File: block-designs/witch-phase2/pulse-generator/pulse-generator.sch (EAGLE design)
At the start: 63 parts, among them IC1 74LVC1G08DBV, IC10 74LVC1G08DBV, IC11 741G175, IC12 74LVC1G08DBV, IC13 741G175, IC14 741G175, IC15 741G175, IC16 74LVC1G04DBV, IC17 741G175, IC18 74LVC1G04DBV, IC19 74LVC1G04DBV, IC2 741G175, IC20 NE555D, IC21 74LVC1G17DBV, IC22 74LVC1G17DBV, IC23 74LVC1G17DBV, IC3 741G175, IC4 741G175, IC5 74LVC1G04DBV, IC6 74LVC1G08DBV, IC7 741G175, IC8 74LVC1G08DBV, IC9 74LVC1G08DBV, J1 POWER_JACKPTH, Q1 MMBT2907ALT1SMD

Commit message: add dekatron sim connector and silkscreen cleanup
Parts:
- added JP3: (no value), pinhead:PINHD-1X4
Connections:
- net 10A_PULSE: now also JP3.2
- net GND: now also J1.GND, J1.GNDBREAK, JP3.4; no longer J1.PWR
- net VCC: now also J1.PWR, JP3.1; no longer J1.GND, J1.GNDBREAK
- net ZC: now also JP3.3
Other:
- moved on the sheet: J1
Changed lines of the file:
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@@
 <layer number="132" name="bAdjust" color="7" fill="1" visible="yes" active="yes"/>
 <layer number="144" name="Drill_legend" color="7" fill="1" visible="yes" active="yes"/>
+<layer number="145" name="DrillLegend_01-16" color="2" fill="9" visible="yes" active="yes"/>
 <layer number="150" name="Notes" color="7" fill="1" visible="yes" active="yes"/>
 <layer number="151" name="HeatSink" color="7" fill="1" visible="yes" active="yes"/>
@@
 <part name="IC23" library="74xx-little-us" deviceset="74*1G17" device="DBV" technology="LVC"/>
 <part name="JP1" library="pinhead" deviceset="PINHD-1X11" device=""/>
+<part name="GND13" library="supply1" deviceset="GND" device=""/>
+<part name="JP3" library="pinhead" deviceset="PINHD-1X4" device=""/>
+<part name="P+17" library="supply1" deviceset="VCC" device=""/>
 </parts>
 <sheets>
@@
 <instance part="FRAME1" gate="G$1" x="0" y="0"/>
 <instance part="FRAME1" gate="G$2" x="299.72" y="0"/>
-<instance part="J1" gate="G$1" x="29.21" y="33.02" rot="MR180"/>
+<instance part="J1" gate="G$1" x="30.48" y="20.32"/>
 <instance part="P+10" gate="VCC" x="41.91" y="39.37" rot="MR0"/>
 <instance part="GND10" gate="1" x="41.91" y="16.51" rot="MR0"/>
@@
 <instance part="IC23" gate="G$1" x="73.66" y="171.45"/>
 <instance part="JP1" gate="A" x="370.84" y="123.19"/>
+<instance part="GND13" gate="1" x="358.14" y="181.61"/>
+<instance part="JP3" gate="A" x="368.3" y="194.31"/>
+<instance part="P+17" gate="VCC" x="358.14" y="209.55"/>
 </instances>
 <busses>
@@
 <net name="VCC" class="0">
 <segment>
-<pinref part="J1" gate="G$1" pin="GNDBREAK"/>
-<wire x1="31.75" y1="27.94" x2="41.91" y2="27.94" width="0.1524" layer="91"/>
-<wire x1="41.91" y1="27.94" x2="41.91" y2="30.48" width="0.1524" layer="91"/>
-<pinref part="J1" gate="G$1" pin="GND"/>
-<wire x1="41.91" y1="30.48" x2="41.91" y2="36.83" width="0.1524" layer="91"/>
-<wire x1="31.75" y1="30.48" x2="41.91" y2="30.48" width="0.1524" layer="91"/>
-<junction x="41.91" y="30.48"/>
-<junction x="41.91" y="27.94"/>
+<wire x1="41.91" y1="27.94" x2="41.91" y2="36.83" width="0.1524" layer="91"/>
 <pinref part="P+10" gate="VCC" pin="VCC"/>
 <pinref part="JP2" gate="G$1" pin="1"/>
 <wire x1="41.91" y1="27.94" x2="50.8" y2="27.94" width="0.1524" layer="91"/>
+<pinref part="J1" gate="G$1" pin="PWR"/>
+<wire x1="41.91" y1="27.94" x2="33.02" y2="27.94" width="0.1524" layer="91"/>
+<junction x="41.91" y="27.94"/>
 </segment>
 <segment>
@@
 <wire x1="33.02" y1="184.15" x2="33.02" y2="186.69" width="0.1524" layer="91"/>
 </segment>
+<segment>
+<wire x1="365.76" y1="199.39" x2="358.14" y2="199.39" width="0.1524" layer="91"/>
+<wire x1="358.14" y1="199.39" x2="358.14" y2="207.01" width="0.1524" layer="91"/>
+<pinref part="JP3" gate="A" pin="1"/>
+<pinref part="P+17" gate="VCC" pin="VCC"/>
+</segment>
 </net>
 <net name="GND" class="0">
 <segment>
-<pinref part="J1" gate="G$1" pin="PWR"/>
-<wire x1="31.75" y1="25.4" x2="41.91" y2="25.4" width="0.1524" layer="91"/>
-<wire x1="41.91" y1="25.4" x2="41.91" y2="19.05" width="0.1524" layer="91"/>
+<wire x1="41.91" y1="25.4" x2="41.91" y2="22.86" width="0.1524" layer="91"/>
 <pinref part="GND10" gate="1" pin="GND"/>
 <pinref part="JP2" gate="G$1" pin="2"/>
+<wire x1="41.91" y1="22.86" x2="41.91" y2="19.05" width="0.1524" layer="91"/>
 <wire x1="41.91" y1="25.4" x2="50.8" y2="25.4" width="0.1524" layer="91"/>
+<pinref part="J1" gate="G$1" pin="GNDBREAK"/>
+<wire x1="41.91" y1="25.4" x2="33.02" y2="25.4" width="0.1524" layer="91"/>
+<pinref part="J1" gate="G$1" pin="GND"/>
+<wire x1="33.02" y1="22.86" x2="41.91" y2="22.86" width="0.1524" layer="91"/>
 <junction x="41.91" y="25.4"/>
+<junction x="41.91" y="22.86"/>
 </segment>
 <segment>
@@
 <junction x="16.51" y="171.45"/>
 </segment>
+<segment>
+<wire x1="358.14" y1="191.77" x2="358.14" y2="184.15" width="0.1524" layer="91"/>
+<pinref part="GND13" gate="1" pin="GND"/>
+<wire x1="358.14" y1="191.77" x2="365.76" y2="191.77" width="0.1524" layer="91"/>
+<pinref part="JP3" gate="A" pin="4"/>
+</segment>
 </net>
 <net name="MCLK" class="0">
@@
 <pinref part="JP1" gate="A" pin="9"/>
 </segment>
+<segment>
+<wire x1="365.76" y1="196.85" x2="336.55" y2="196.85" width="0.1524" layer="91"/>
+<label x="336.55" y="196.85" size="1.778" layer="95"/>
+<pinref part="JP3" gate="A" pin="2"/>
+</segment>
 </net>
 <net name="!RST" class="0">
@@
 </segment>
 </net>
+<net name="ZC" class="0">
+<segment>
+<pinref part="JP3" gate="A" pin="3"/>
+<wire x1="365.76" y1="194.31" x2="336.55" y2="194.31" width="0.1524" layer="91"/>
+<label x="336.55" y="194.31" size="1.778" layer="95"/>
+</segment>
+</net>

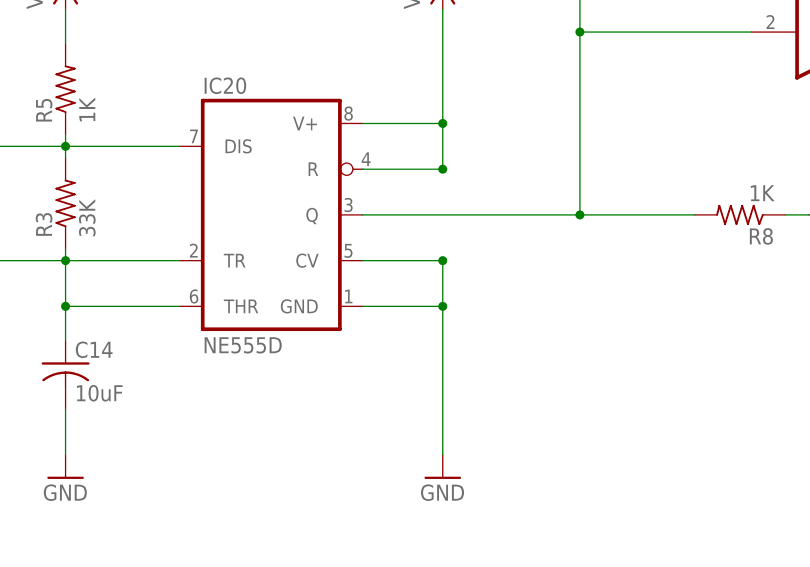
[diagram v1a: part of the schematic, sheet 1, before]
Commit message: remove connection to pin5 on 555
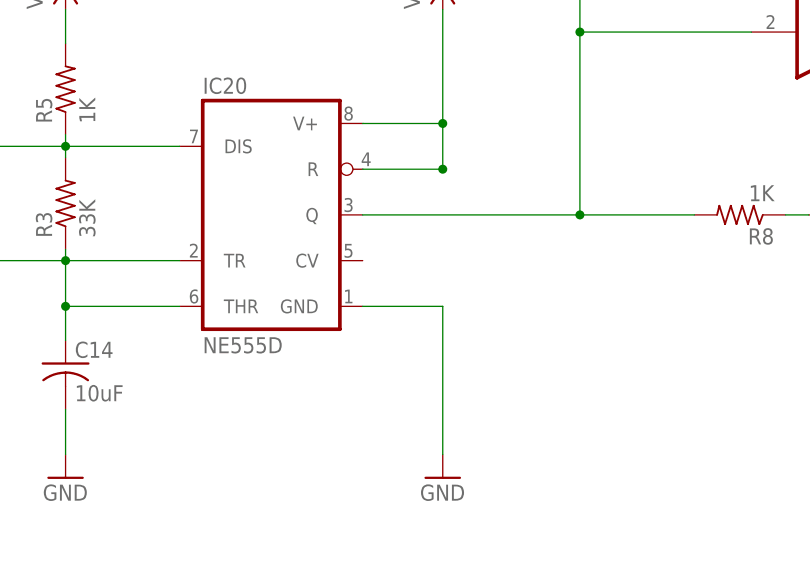
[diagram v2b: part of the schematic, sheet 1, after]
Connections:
- net GND: no longer IC20.CV
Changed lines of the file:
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@@
 </segment>
 <segment>
-<pinref part="IC20" gate="A" pin="CV"/>
 <pinref part="GND6" gate="1" pin="GND"/>
-<wire x1="205.74" y1="160.02" x2="214.63" y2="160.02" width="0.1524" layer="91"/>
-<wire x1="214.63" y1="160.02" x2="214.63" y2="154.94" width="0.1524" layer="91"/>
 <pinref part="IC20" gate="A" pin="GND"/>
 <wire x1="214.63" y1="154.94" x2="214.63" y2="138.43" width="0.1524" layer="91"/>
 <wire x1="205.74" y1="154.94" x2="214.63" y2="154.94" width="0.1524" layer="91"/>
-<junction x="214.63" y="160.02"/>
-<junction x="214.63" y="154.94"/>
 </segment>
 <segment>

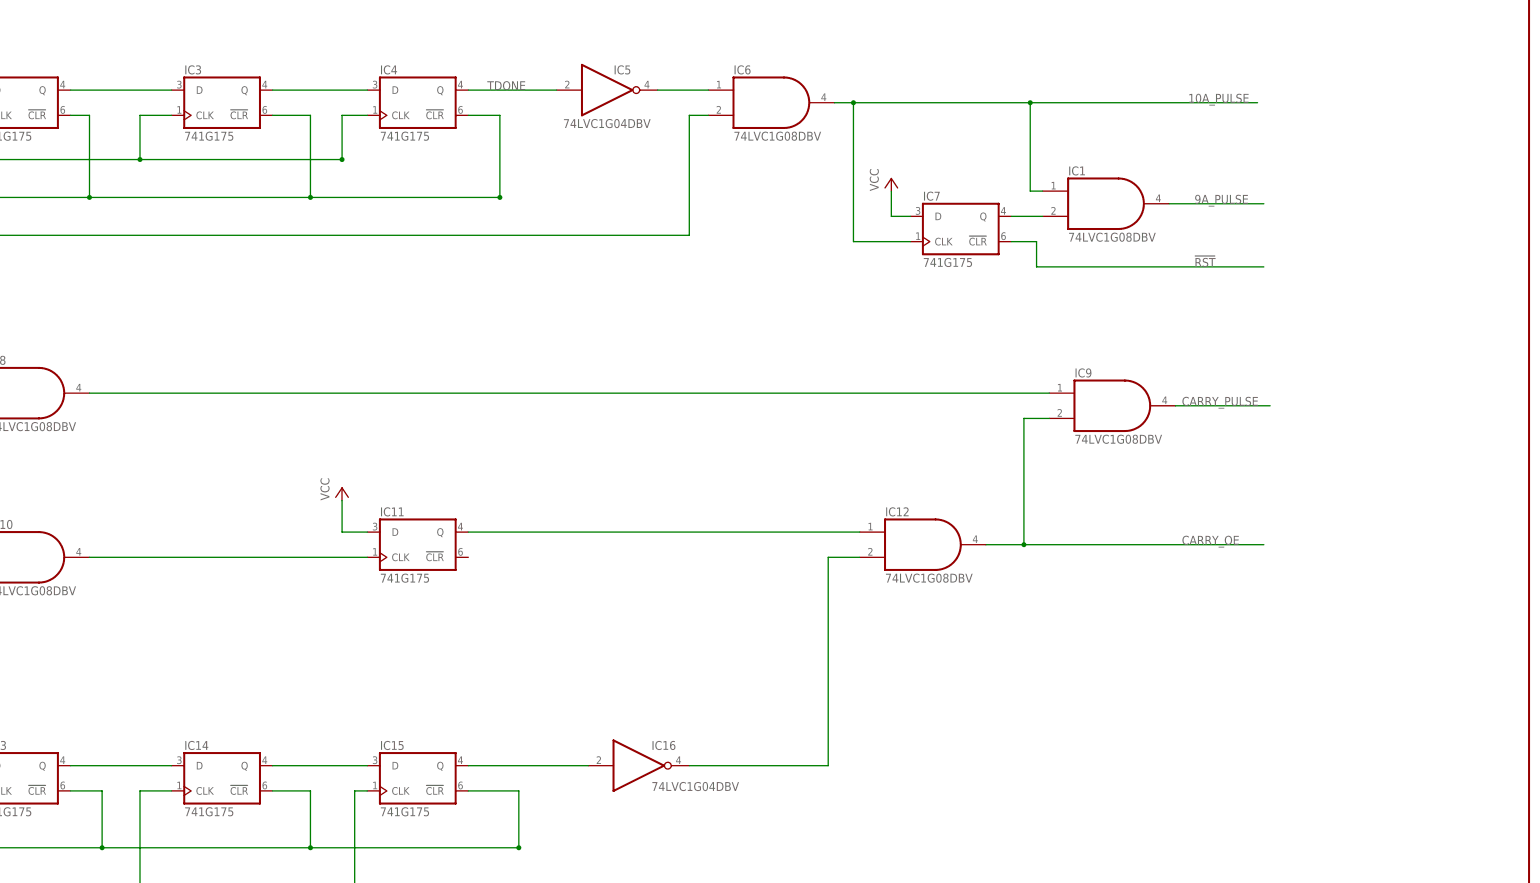
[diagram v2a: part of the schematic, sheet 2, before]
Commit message: fix pin5 on 555, invert 9A latch, connect !RST to TCLK flip-flop
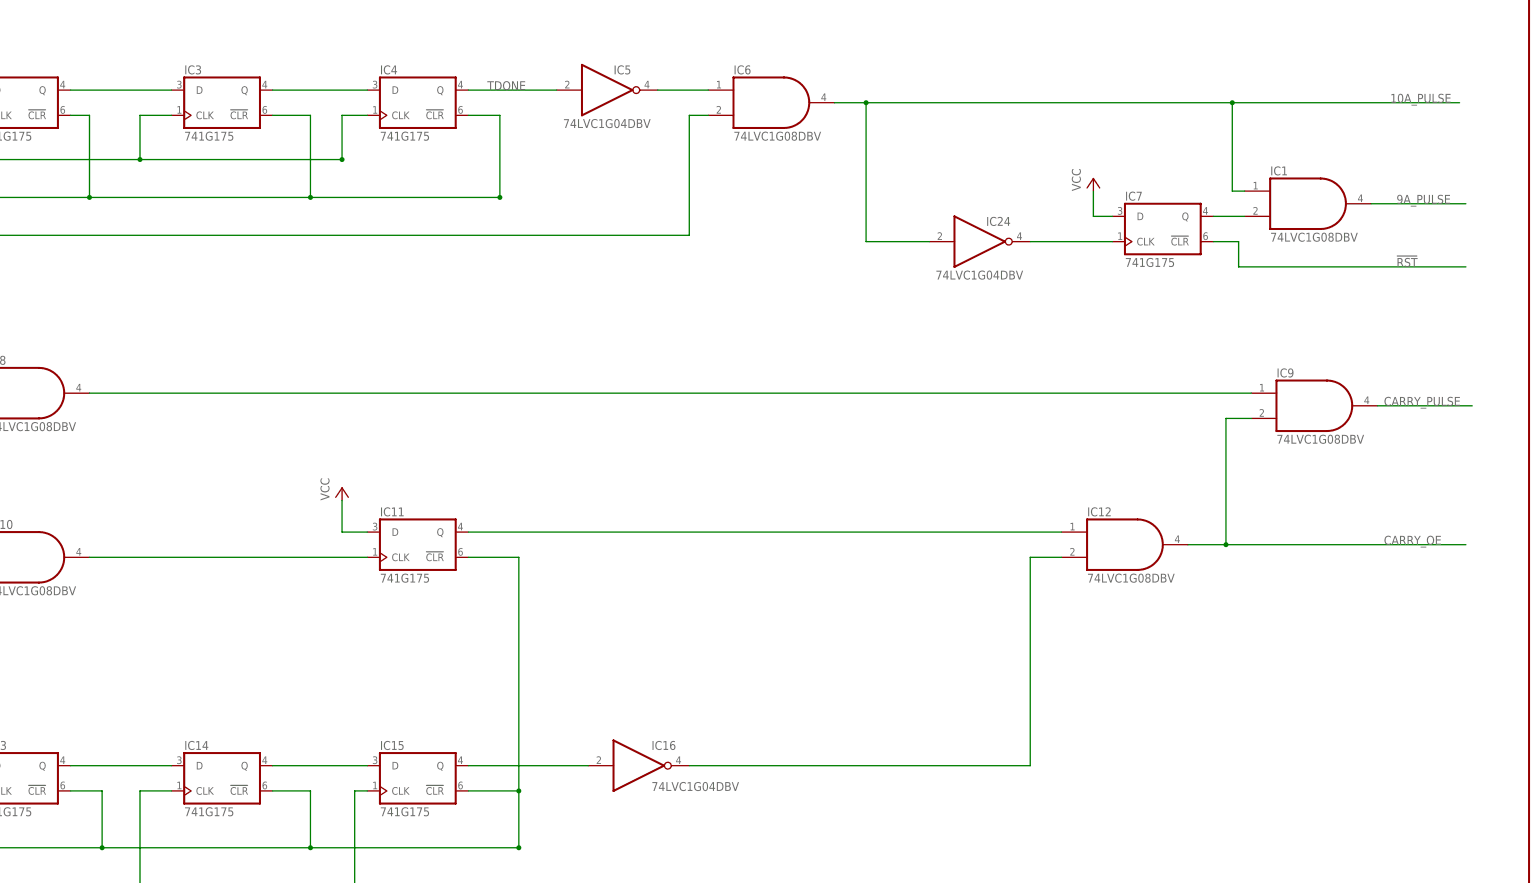
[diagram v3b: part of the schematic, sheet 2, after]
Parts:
- removed C15: 10uF, resistor:C-USC0805
- removed R1: 1K, resistor:R-US_R0805
- added IC24: 74LVC1G04DBV, 74xx-little-us:74LVC1G04DBV
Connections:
- removed net N$10: C15.1, IC17G$1.!CLR, R1.1
- new net N$23: IC24A.O, IC7G$1.CLK
- net !RST: now also IC11G$1.!CLR, IC17G$1.!CLR
- net 10A_PULSE: now also IC24A.I; no longer IC7G$1.CLK
- net GND: no longer C15.2
- net VCC: no longer R1.2
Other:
- moved on the sheet: IC1, IC12, IC7, IC9

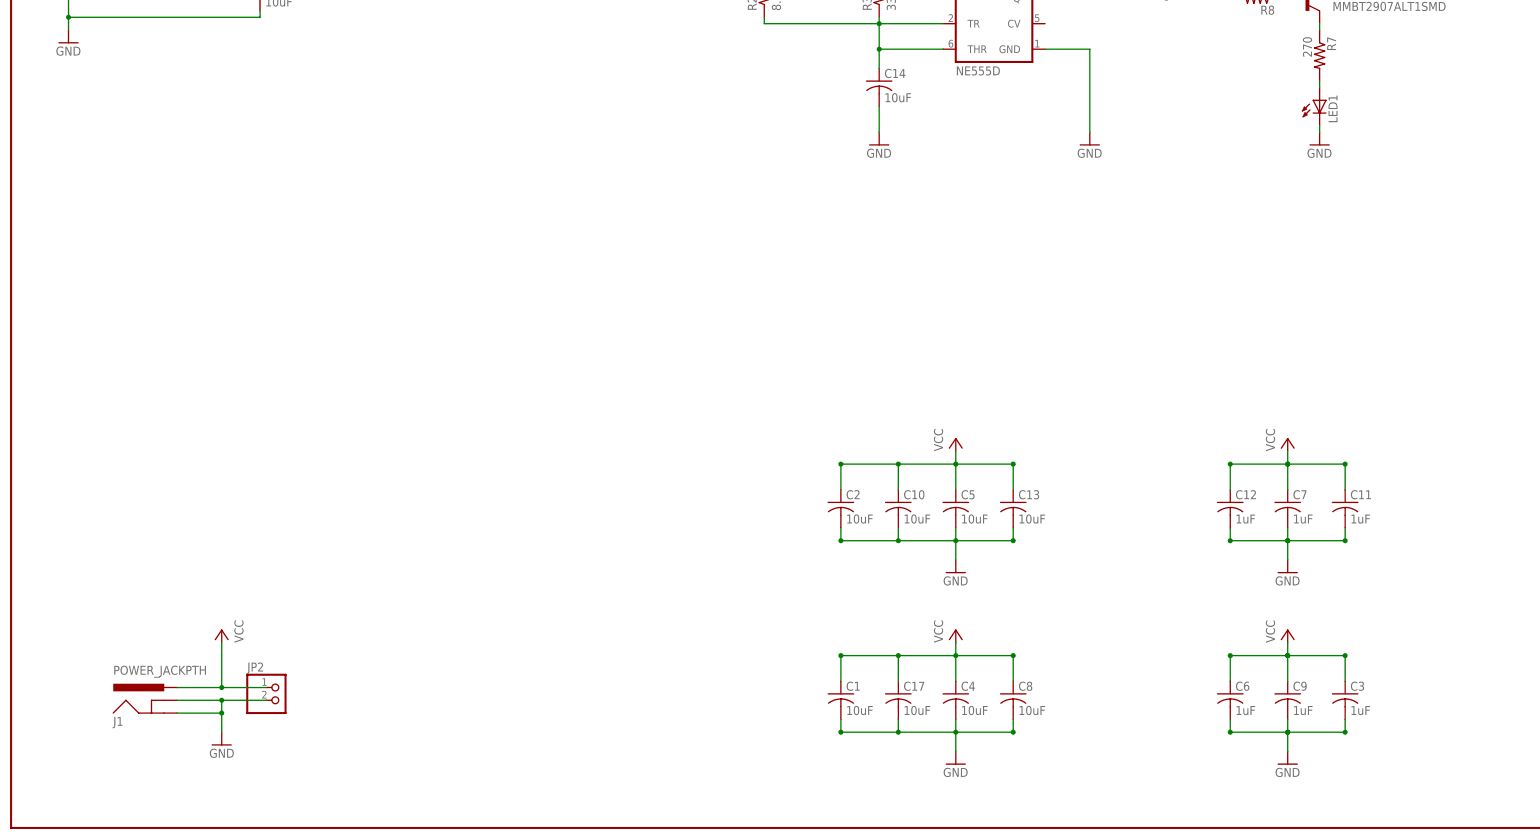
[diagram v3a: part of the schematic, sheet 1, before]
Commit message: add additional bypass caps and LEDs for signals
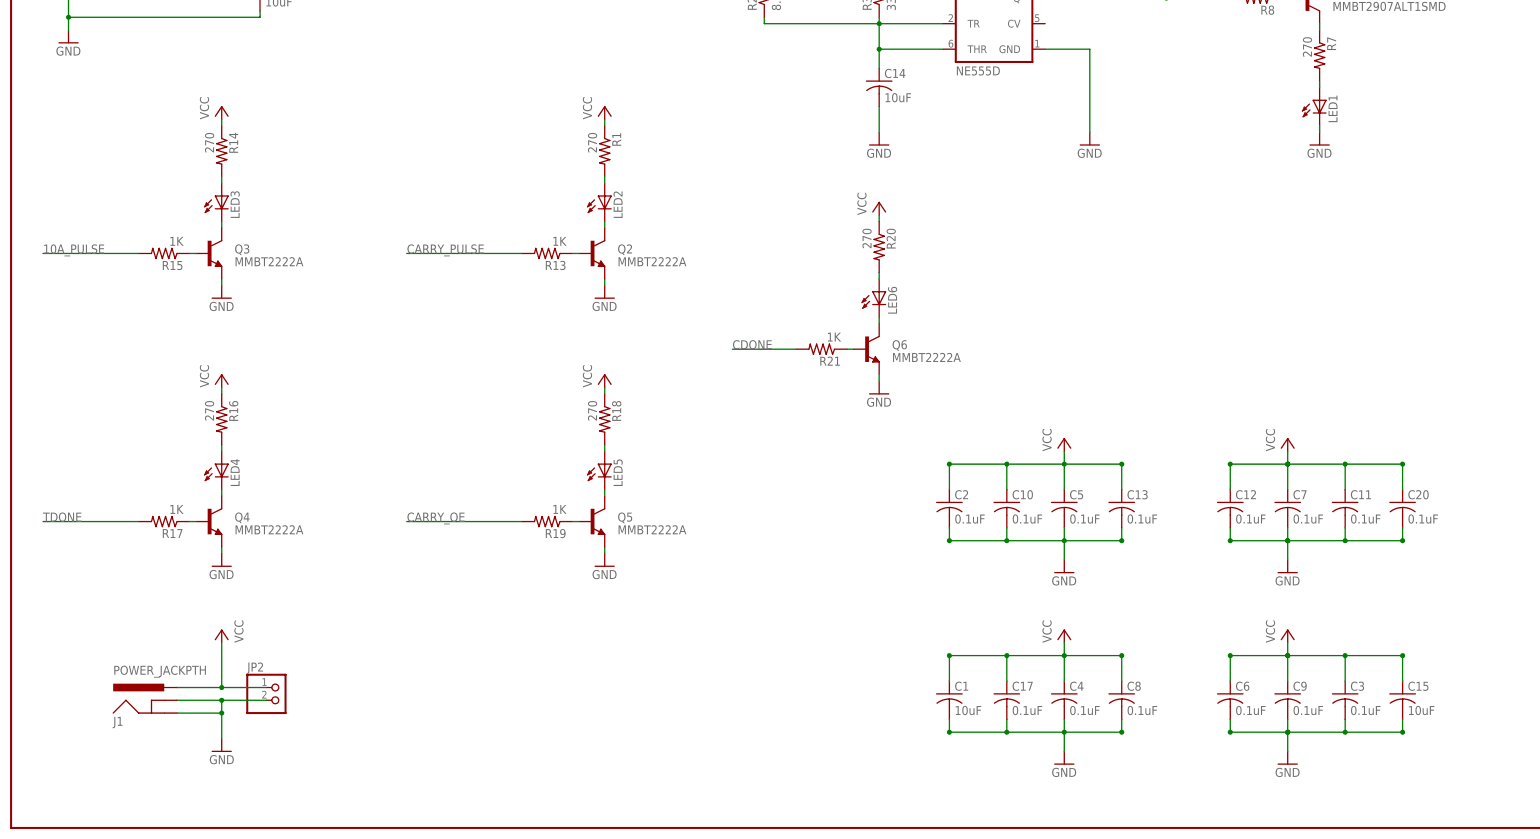
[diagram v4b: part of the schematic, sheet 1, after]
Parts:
- added C15: 10uF, resistor:C-USC0805
- added C20, C21, C22, C23, C24, C25, C26, C27: 0.1uF, resistor:C-USC0805
- added LED2, LED3, LED4, LED5, LED6: (no value), led:LEDCHIP-LED0805
- added Q2, Q3, Q4, Q5, Q6: MMBT2222A, SparkFun-DiscreteSemi:TRANSISTOR_NPNMMBT2222A
- added R1, R14, R16, R18, R20: 270, resistor:R-US_R0805
- added R13, R15, R17, R19, R21: 1K, resistor:R-US_R0805
- C10, C13, C17, C2, C4, C5, C8: value 10uF -> 0.1uF
- C11, C12, C3, C6, C7, C9: value 1uF -> 0.1uF
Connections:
- net N$13 renamed !CDONE
- removed net N$18: IC15G$1.Q, IC16A.I
- new net CDONE: IC15G$1.Q, IC16A.I, R21.2
- new net N$10: LED2.C, Q2.C
- new net N$13: LED3.C, Q3.C
- new net N$24: Q2.B, R13.1
- new net N$25: LED2.A, R1.2
- new net N$26: Q3.B, R15.1
- new net N$28: LED3.A, R14.2
- new net N$31: LED4.C, Q4.C
- new net N$32: Q4.B, R17.1
- new net N$33: LED4.A, R16.2
- new net N$34: LED5.C, Q5.C
- new net N$35: Q5.B, R19.1
- new net N$36: LED5.A, R18.2
- new net N$37: LED6.C, Q6.C
- new net N$38: Q6.B, R21.1
- new net N$39: LED6.A, R20.2
- net 10A_PULSE: now also R15.2
- net CARRY_OE: now also R19.2
- net CARRY_PULSE: now also R13.2
- net GND: now also C15.2, C20.2, C21.2, C22.2, C23.2, C24.2, C25.2, C26.2, C27.2, Q2.E, Q3.E, Q4.E, Q5.E, Q6.E
- net TDONE: now also R17.2
- net VCC: now also C15.1, C20.1, C21.1, C22.1, C23.1, C24.1, C25.1, C26.1, C27.1, R1.1, R14.1, R16.1, R18.1, R20.1
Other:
- moved on the sheet: C1, C10, C13, C17, C2, C4, C5, C8
